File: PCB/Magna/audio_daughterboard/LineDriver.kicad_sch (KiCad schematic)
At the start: 31 parts, among them J701 PSG01550, Q701 NMOS, Q702 NMOS, U701 NE5532

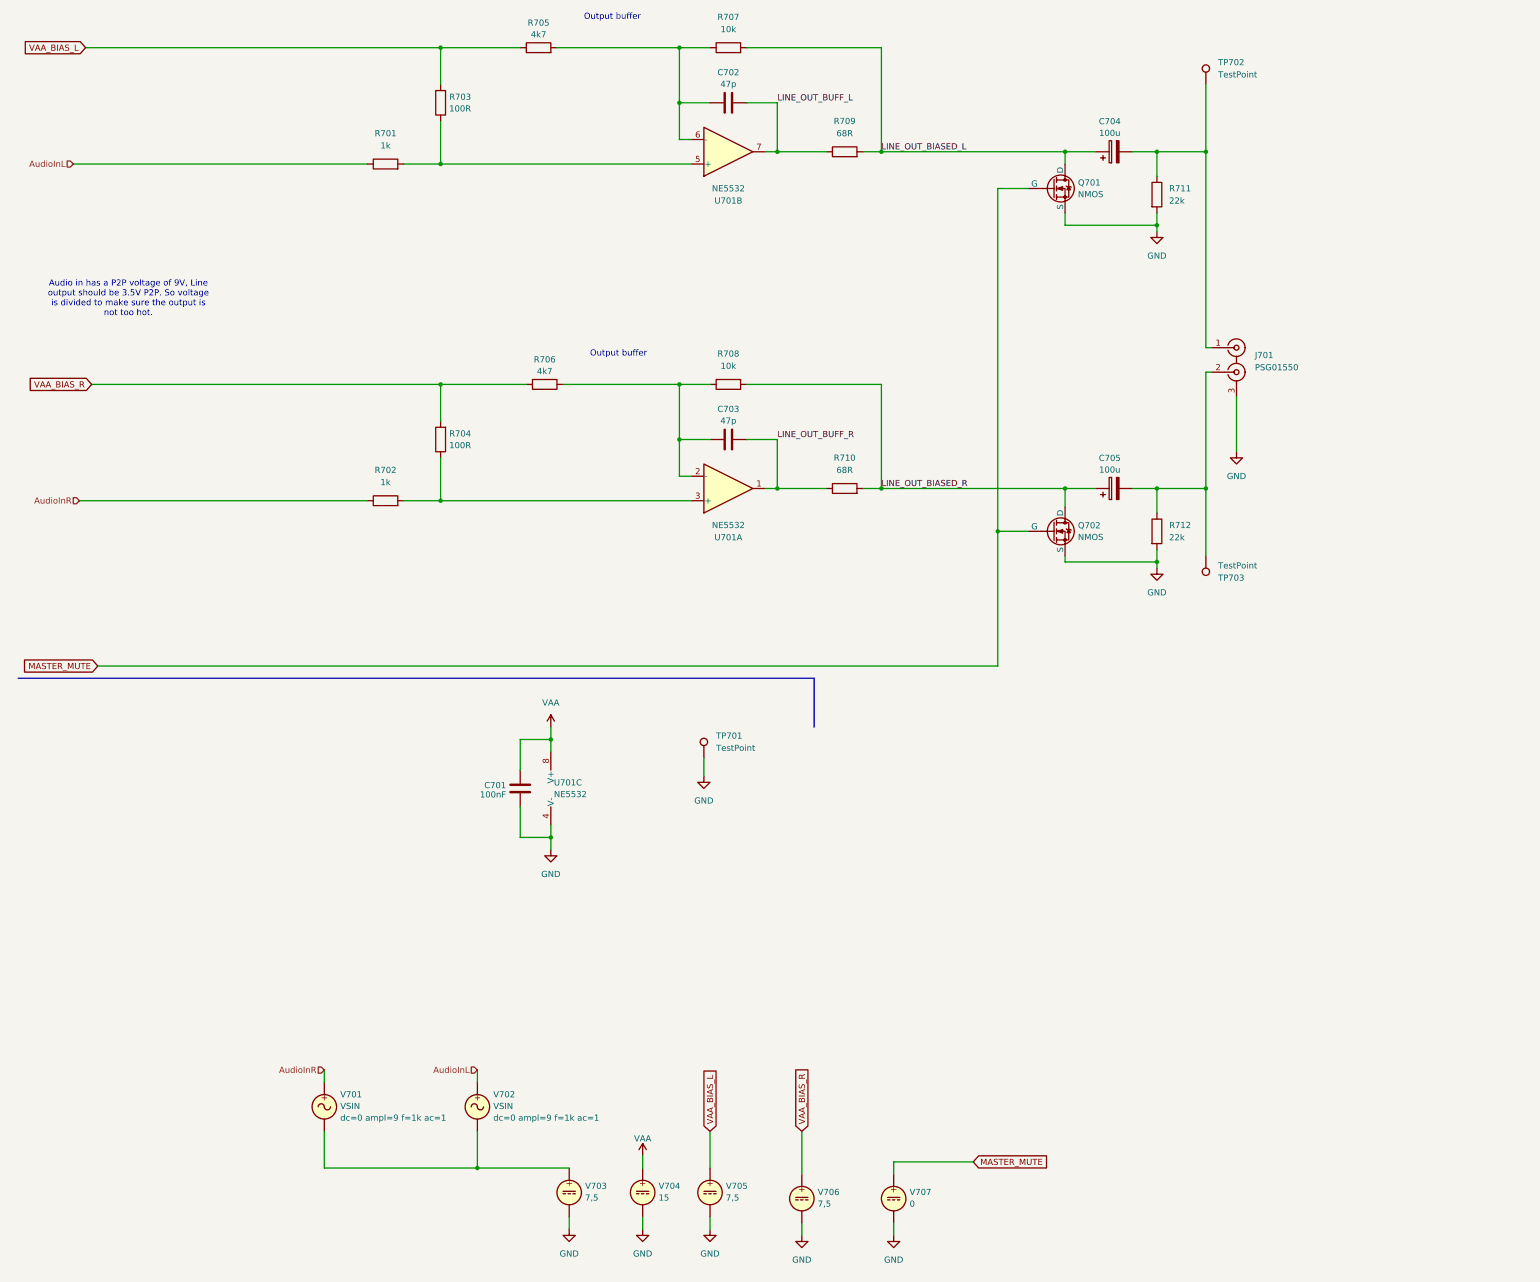
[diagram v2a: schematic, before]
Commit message: Start layout and routing of Audio Daugherboard
Also a lot of small changes to everything that became apperant
when the audio daughterboard was designed. Such as the Headphone
PCB, which is now separate from the rest of the audio.
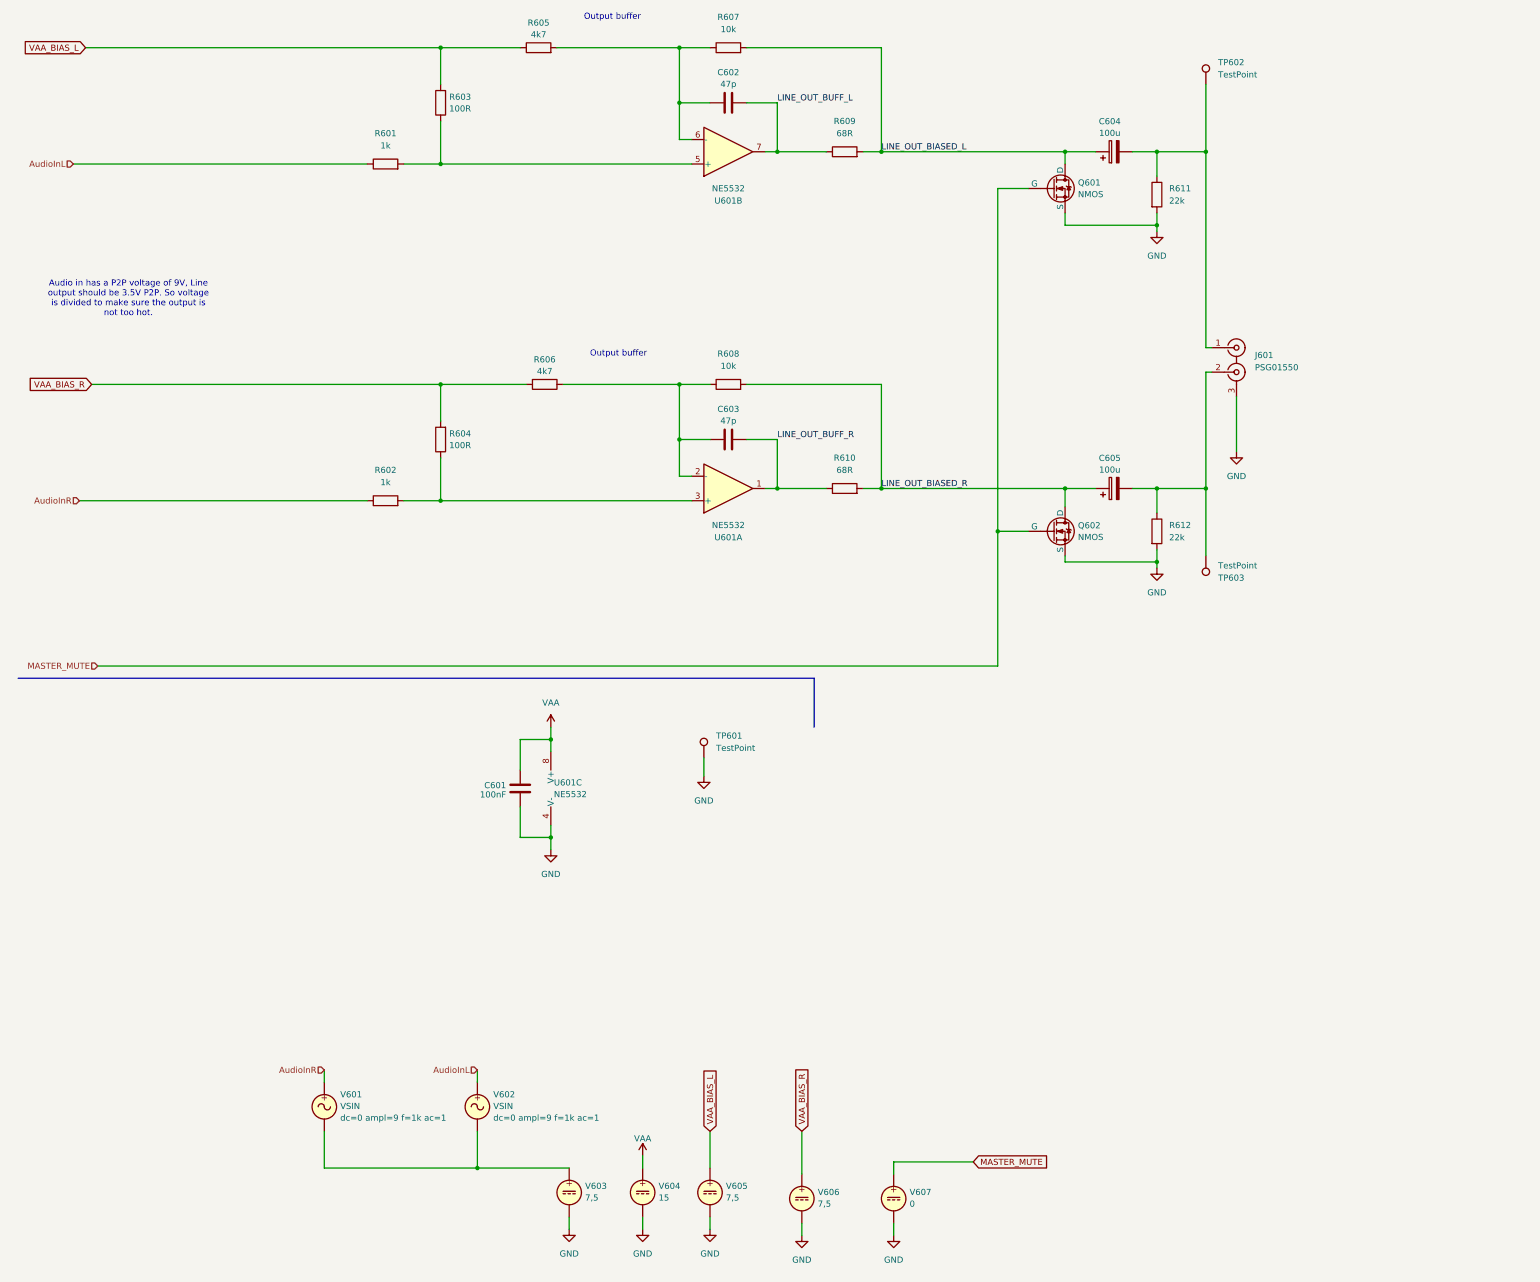
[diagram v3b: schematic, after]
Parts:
- renumbered C701 to C601, C702 to C602, C703 to C603, C704 to C604, C705 to C605, J701 to J601, Q701 to Q601, Q702 to Q602, R701 to R601, R702 to R602, R703 to R603, R704 to R604, R705 to R605, R706 to R606, R707 to R607, R708 to R608, R709 to R609, R710 to R610, R711 to R611, R712 to R612, TP701 to TP601, TP702 to TP602, TP703 to TP603, U701 to U601, V701 to V601, V702 to V602, V703 to V603, V704 to V604, V705 to V605, V706 to V606, V707 to V607

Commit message: Finished first round of routing for the Audio Daughterboard
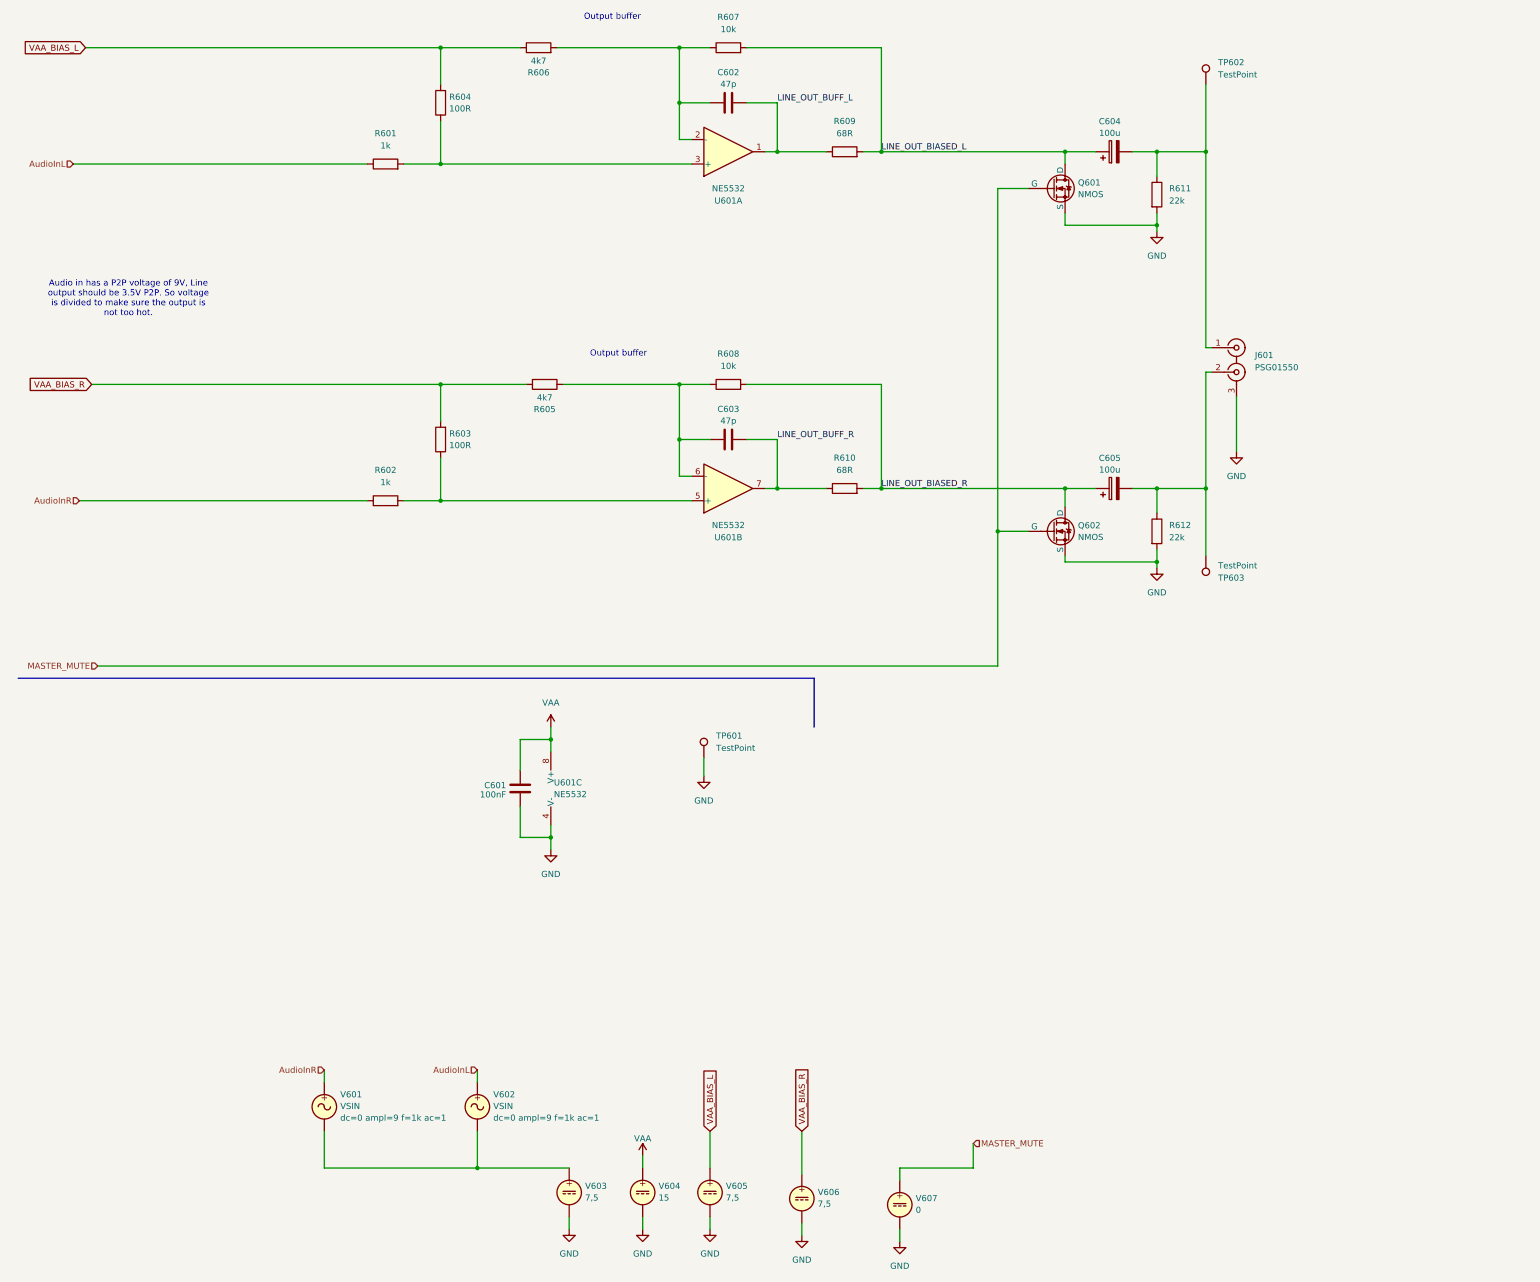
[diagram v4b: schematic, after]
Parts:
- R601, R602, R603, R604, R605, R606, R607, R608, R609, R610, R611, R612: now in the parts list
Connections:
- net LINE_OUT_BUFF_L: now also U601.1; no longer U601.7
- net LINE_OUT_BUFF_R: now also U601.7; no longer U601.1
- net VAA_BIAS_L: now also R604.2, R606.1; no longer R603.2, R605.1
- net VAA_BIAS_R: now also R603.2, R605.2; no longer R604.2, R606.2
- net at R604.1, U601.3 (+): now also R601.2; no longer R602.2
- net at R603.1, U601.5 (+): now also R602.2; no longer R601.2
- net at C602.1, R607.1: now also R606.2, U601.2 (-); no longer R605.2, U601.6 (-)
- net at C603.1, R608.1: now also R605.1, U601.6 (-); no longer R606.1, U601.2 (-)
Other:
- moved on the sheet: R603, R604, R605, R606, U601A, U601B, V607
